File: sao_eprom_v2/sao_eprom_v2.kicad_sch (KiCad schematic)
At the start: 44 parts, among them J1 Conn_01x03, J2 USB_C_Receptacle_USB2.0, J3 sao_v2_addon_tht, J4 Conn_01x02, J5 I2C, J6 I2C, U1 W25Q128JVS, U2 RP2040, U3 24LC00, X1 SX3M12.000M20F30TNN

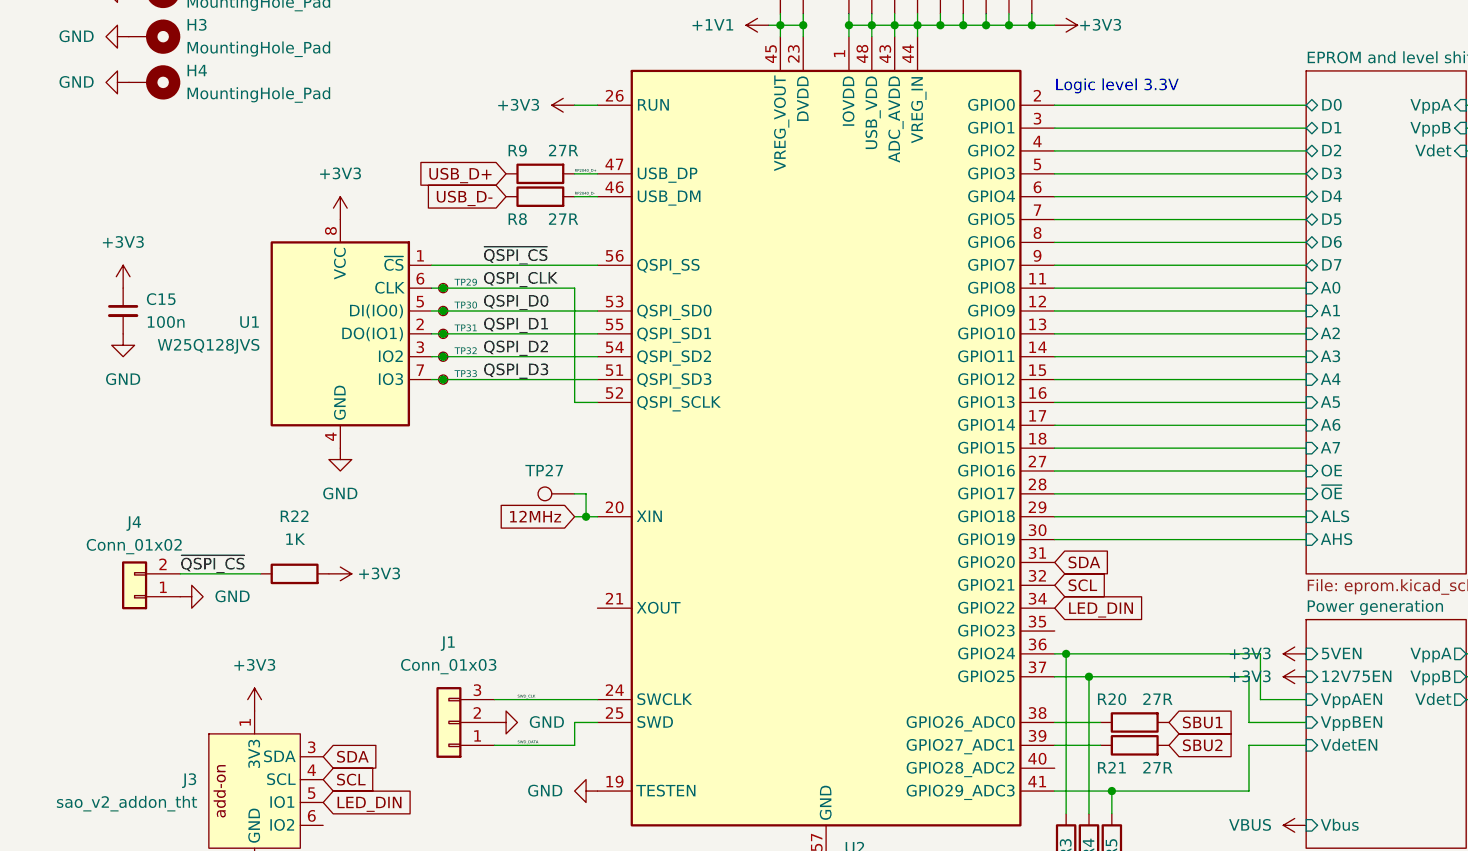
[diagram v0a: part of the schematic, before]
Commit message: Put yet another feedback in my design
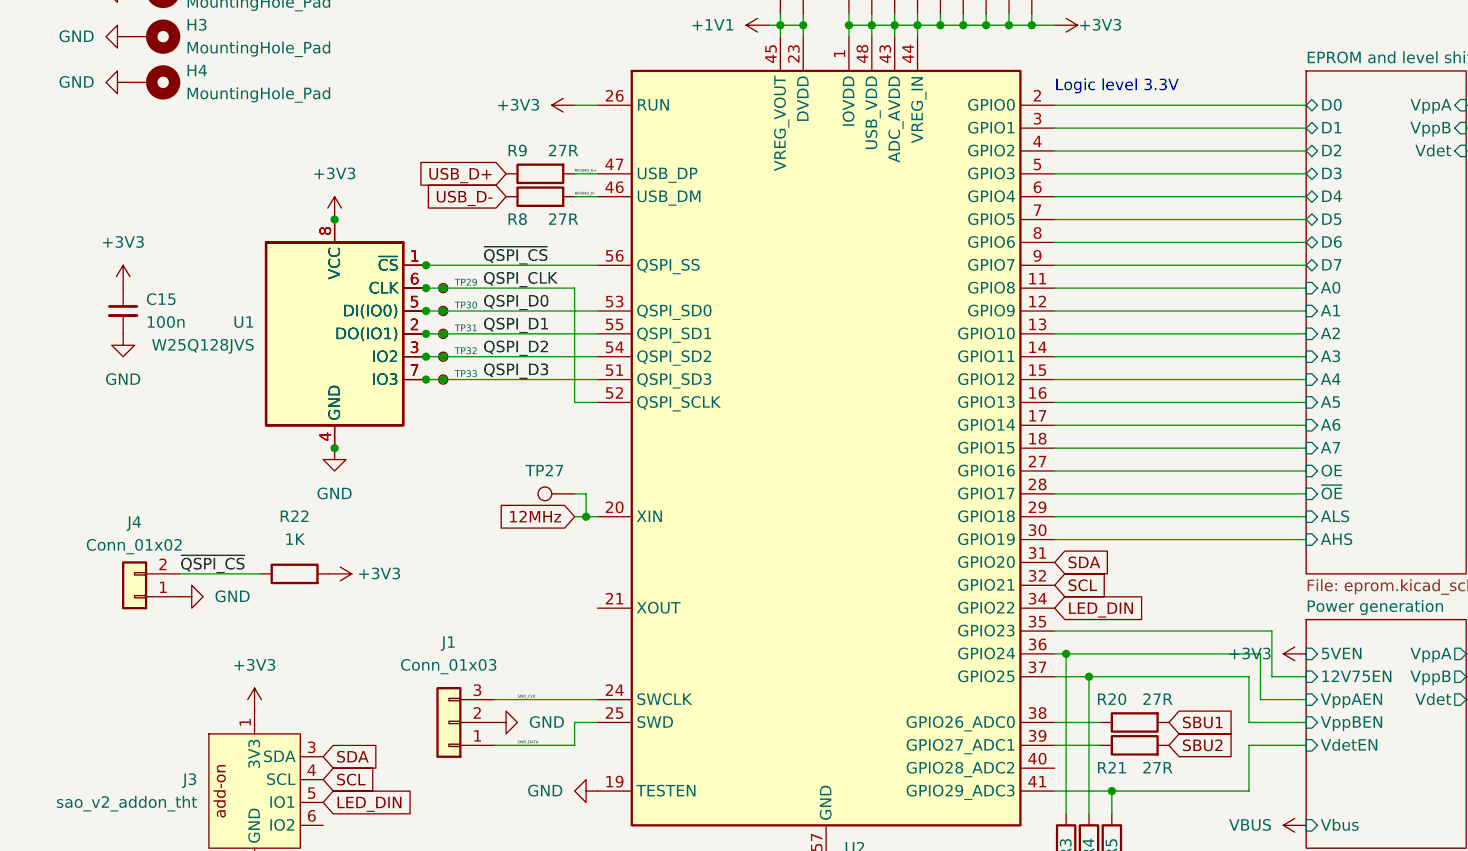
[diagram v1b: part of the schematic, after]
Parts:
- added U11: W25Q16JVUXIQ, flash:PSON50P300X200X60-9N, symbol Memory_Flash:W25Q128JVS
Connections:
- net +3V3: now also U11.8 (VCC)
- net GND: now also U11.4 (GND)
- net QSPI_CLK: now also U11.6 (CLK)
- net QSPI_D0: now also U11.5 (DI(IO0))
- net QSPI_D1: now also U11.2 (DO(IO1))
- net QSPI_D2: now also U11.3 (IO2)
- net QSPI_D3: now also U11.7 (IO3)
- net ~{QSPI_CS}: now also U11.1 (~{CS})
- net Power generation/12V75EN: now reaches U2.35 (GPIO23)
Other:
- moved on the sheet: U1

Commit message: Candidate revision No. 1
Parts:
- removed C23: 100n, Capacitor_SMD:C_0402_1005Metric_Pad0.74x0.62mm_HandSolder, symbol Device:C_Small
- removed TP27: TestPoint, TestPoint:TestPoint_Pad_D1.0mm, symbol Connector:TestPoint
- removed X1: SX3M12.000M20F30TNN, Crystal:Crystal_SMD_3225-4Pin_3.2x2.5mm, symbol oscillator:YSO110TR
- added C23, C29: 22p, Capacitor_SMD:C_0402_1005Metric_Pad0.74x0.62mm_HandSolder, symbol mch2021-rescue:C-Device
- added R23: 1k, Resistor_SMD:R_0402_1005Metric_Pad0.72x0.64mm_HandSolder, symbol mch2021-rescue:R-Device
- added Y1: 12MHz, Crystal:Crystal_SMD_3225-4Pin_3.2x2.5mm, symbol mch2021-rescue:Crystal_GND24_Small-Device
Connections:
- net GND: now also C23.2, C29.2, Y1.2, Y1.4
- net at U2.21 (XOUT): now also R23.2
- net 12MHz: no longer names the net of U2.20 (XIN)
- net 12MHz: now also C29.1, Y1.1
- new net: C23.1, R23.1, Y1.3
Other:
- moved on the sheet: J3, J4, R22

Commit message: More EPROM devving
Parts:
- removed J1: Conn_01x03, Connector_PinHeader_2.54mm:PinHeader_1x03_P2.54mm_Vertical, symbol Connector_Generic:Conn_01x03
- removed R20, R21: 27R, Resistor_SMD:R_0402_1005Metric_Pad0.72x0.64mm_HandSolder, symbol Device:R
- added J1: Conn_01x04, Connector_PinHeader_2.54mm:PinHeader_1x04_P2.54mm_Vertical, symbol Connector_Generic:Conn_01x04
- added R24: 10K, Resistor_SMD:R_0402_1005Metric_Pad0.72x0.64mm_HandSolder, symbol Device:R
- renumbered R22 to R20, R23 to R21
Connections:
- net +3V3: now also R20.1; no longer R20.2
- net GND: now also J1.3 (Pin_3), R24.2
- net SWD_CLK: now also J1.4 (Pin_4)
- net SWD_DATA: now also J1.2 (Pin_2)
- net ~{QSPI_CS}: now also R20.2, J1.1 (Pin_1); no longer J4.2 (Pin_2), R20.1
- net Power generation/VLEDEN: now reaches U2.38 (GPIO26_ADC0)
- net Power generation/VLEDEN: now also R24.1
- net SBU1: no longer names the net of J2.A8 (SBU1)
- net SBU2: no longer names the net of J2.B8 (SBU2)
- new net Power generation/VLED: J4.2 (Pin_2)
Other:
- sheet Power generation ports: added VLED, VLEDEN; removed none
- moved on the sheet: R20, TP29, TP30, TP31, TP32, TP33

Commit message: Remove mounting holes from BOM
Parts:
- H1, H2, H3, H4: now left out of the parts list
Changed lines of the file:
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@@
   )
   (symbol (lib_id "Mechanical:MountingHole_Pad") (at 27.94 29.21 270) (unit 1)
-    (in_bom yes) (on_board yes) (dnp no) (fields_autoplaced)
+    (in_bom no) (on_board yes) (dnp no) (fields_autoplaced)
     (property "Reference" "H2" (at 31.75 27.94 90)
       (effects (font (size 1.27 1.27)) (justify left))
@@
   )
   (symbol (lib_id "Mechanical:MountingHole_Pad") (at 27.94 34.29 270) (unit 1)
-    (in_bom yes) (on_board yes) (dnp no) (fields_autoplaced)
+    (in_bom no) (on_board yes) (dnp no) (fields_autoplaced)
     (property "Reference" "H3" (at 31.75 33.02 90)
       (effects (font (size 1.27 1.27)) (justify left))
@@
   )
   (symbol (lib_id "Mechanical:MountingHole_Pad") (at 27.94 39.37 270) (unit 1)
-    (in_bom yes) (on_board yes) (dnp no) (fields_autoplaced)
+    (in_bom no) (on_board yes) (dnp no) (fields_autoplaced)
     (property "Reference" "H4" (at 31.75 38.1 90)
       (effects (font (size 1.27 1.27)) (justify left))
@@
   )
   (symbol (lib_id "Mechanical:MountingHole_Pad") (at 27.94 24.13 270) (unit 1)
-    (in_bom yes) (on_board yes) (dnp no) (fields_autoplaced)
+    (in_bom no) (on_board yes) (dnp no) (fields_autoplaced)
     (property "Reference" "H1" (at 31.75 22.86 90)
       (effects (font (size 1.27 1.27)) (justify left))
